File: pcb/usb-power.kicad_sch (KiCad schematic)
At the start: 7 parts, among them J2 USB4105, U3 NCP1117-3.3_SOT223

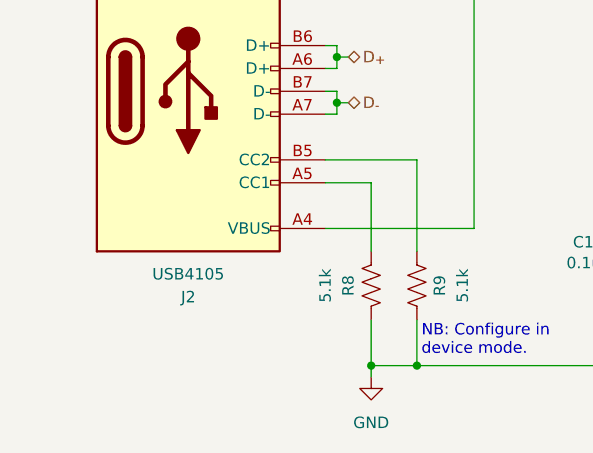
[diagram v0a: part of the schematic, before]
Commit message: Replaced through-hole components with SMD
- Other small edits (e.g. optional jumper to force USB-boot)
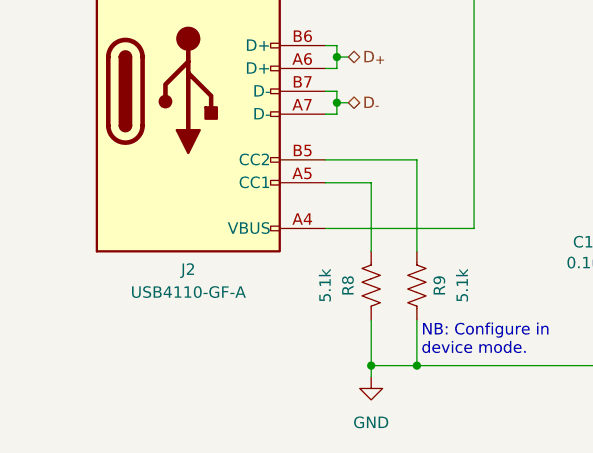
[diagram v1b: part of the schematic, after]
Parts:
- J2: value USB4105 -> USB4110-GF-A; footprint Connector_USB:USB_C_Receptacle_GCT_USB4105-xx-A_16P_TopMnt_Horizontal -> Connector_USB:USB_C_Receptacle_GCT_USB4110
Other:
- company: (none) -> Open Ephys, Inc.
- title: (none) -> Open Ephys Commutator Controller
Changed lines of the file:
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@@
 	(generator_version "8.0")
 	(paper "A5")
+	(title_block
+		(title "Open Ephys Commutator Controller")
+		(rev "D")
+		(company "Open Ephys, Inc.")
+	)
 	(junction
 		(at 88.9 41.91)
@@
 		(dnp no)
 		(property "Reference" "J2"
-			(at 57.15 86.36 0)
-			(effects
-				(font
-					(size 1.27 1.27)
-				)
-			)
-		)
-		(property "Value" "USB4105"
-			(at 57.15 83.82 0)
-			(effects
-				(font
-					(size 1.27 1.27)
-				)
-			)
-		)
-		(property "Footprint" "Connector_USB:USB_C_Receptacle_GCT_USB4105-xx-A_16P_TopMnt_Horizontal"
+			(at 57.15 83.312 0)
+			(effects
+				(font
+					(size 1.27 1.27)
+				)
+			)
+		)
+		(property "Value" "USB4110-GF-A"
+			(at 57.15 85.852 0)
+			(effects
+				(font
+					(size 1.27 1.27)
+				)
+			)
+		)
+		(property "Footprint" "Connector_USB:USB_C_Receptacle_GCT_USB4110"
 			(at 60.96 63.5 0)
 			(effects

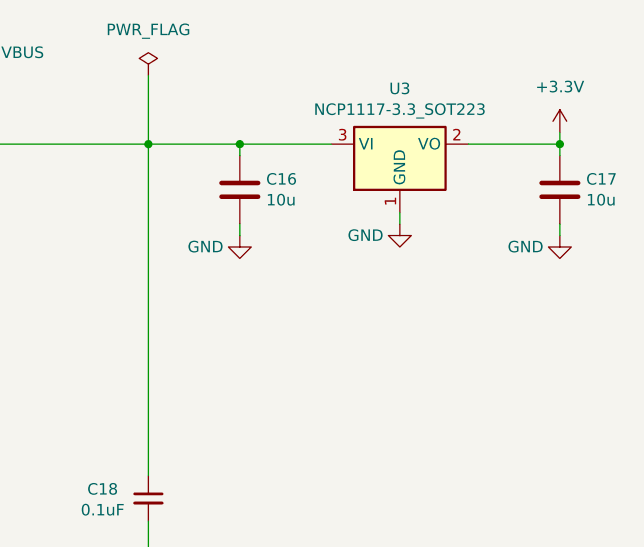
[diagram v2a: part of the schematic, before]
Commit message: Revision D of controller PCB
- Small changes during PCB review
- This commit will be fabricated
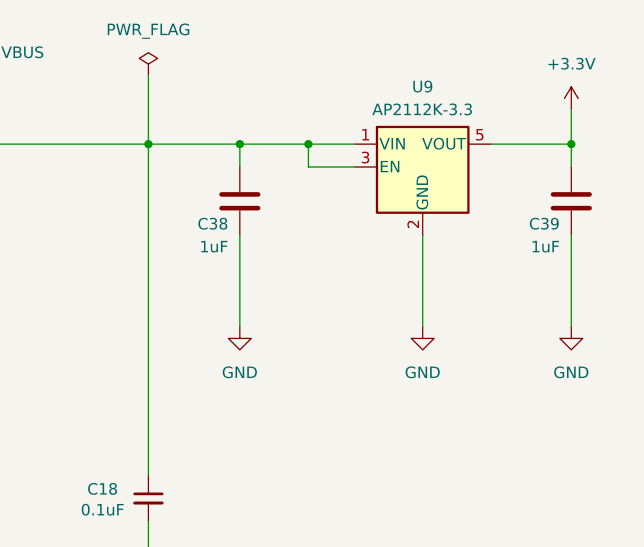
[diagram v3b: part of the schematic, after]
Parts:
- removed C16, C17: 10u, Capacitor_SMD:C_0805_2012Metric, symbol Device:C
- removed U3: NCP1117-3.3_SOT223, Package_TO_SOT_SMD:SOT-223-3_TabPin2, symbol Regulator_Linear:NCP1117-3.3_SOT223
- added C38, C39: 1uF, Capacitor_SMD:C_0603_1608Metric, symbol Device:C
- added U9: AP2112K-3.3, Package_TO_SOT_SMD:SOT-23-5, symbol Regulator_Linear:AP2112K-3.3
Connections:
- net +3.3V: now also C39.1, U9.5 (VOUT)
- net GND: now also C38.2, C39.2, U9.2 (GND)
- net VBUS: now also C38.1, U9.1 (VIN), U9.3 (EN)
